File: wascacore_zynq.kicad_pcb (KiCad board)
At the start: 4 copper layers, 67.6 x 31.1 mm, 51 parts, among them J1 SODIMM-200, U1 DDR3, U2 xc7z010clg400

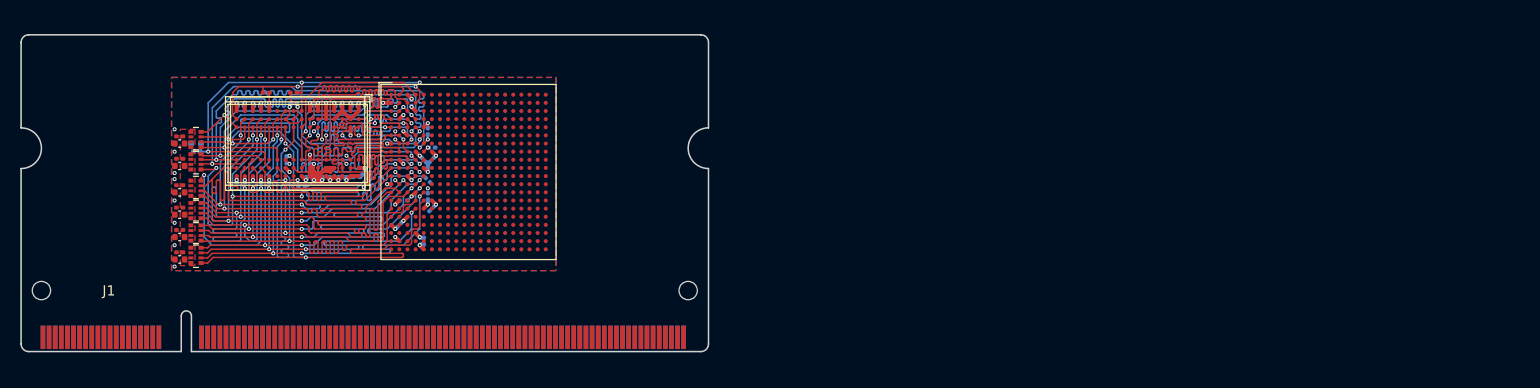
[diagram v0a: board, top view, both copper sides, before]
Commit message: SDRAM added
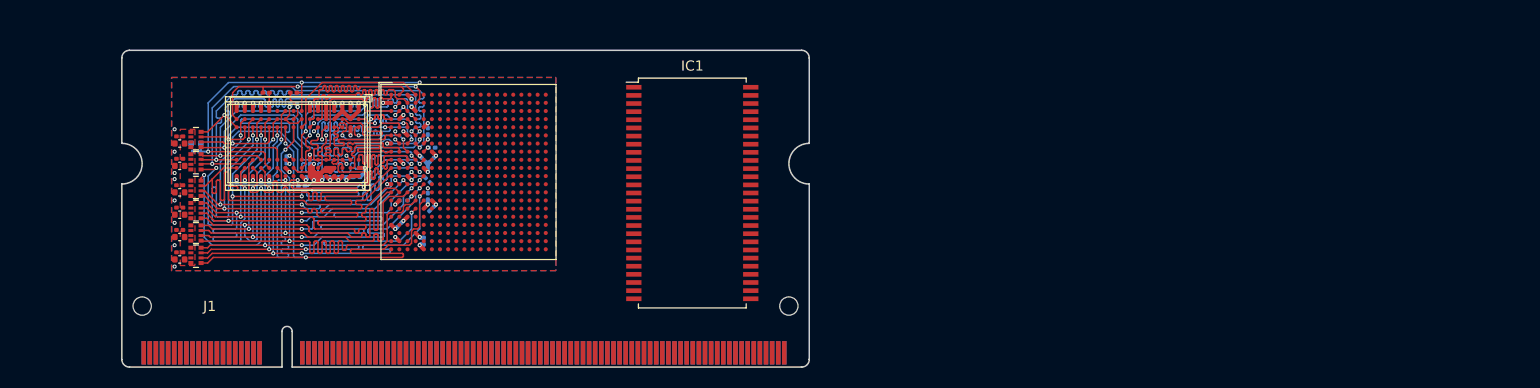
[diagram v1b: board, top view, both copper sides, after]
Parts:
- added IC1: SDRAM_MT48_x16, Package_SO:TSOP-II-54_22.2x10.16mm_P0.8mm, F.Cu at (72.0, 15.4)
- moved J1 10.0 mm to (15.9, 32.5)
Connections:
- U2 pad A10: (no net) -> Net-(U2-PadA10)
- U2 pad A11: (no net) -> Net-(U2-PadA11)
- U2 pad A12: (no net) -> Net-(U2-PadA12)
- U2 pad A13: (no net) -> Net-(U2-PadA13)
- U2 pad A14: (no net) -> Net-(U2-PadA14)
- U2 pad A15: (no net) -> Net-(U2-PadA15)
- U2 pad A16: (no net) -> Net-(U2-PadA16)
- U2 pad A17: (no net) -> Net-(U2-PadA17)
- U2 pad A19: (no net) -> Net-(U2-PadA19)
- U2 pad A20: (no net) -> Net-(U2-PadA20)
- U2 pad A5: (no net) -> Net-(U2-PadA5)
- U2 pad A6: (no net) -> Net-(U2-PadA6)
- U2 pad A7: (no net) -> Net-(U2-PadA7)
- U2 pad A9: (no net) -> Net-(U2-PadA9)
- U2 pad B10: (no net) -> Net-(U2-PadB10)
- U2 pad B12: (no net) -> Net-(U2-PadB12)
- U2 pad B13: (no net) -> Net-(U2-PadB13)
- U2 pad B14: (no net) -> Net-(U2-PadB14)
- U2 pad B15: (no net) -> Net-(U2-PadB15)
- U2 pad B16: (no net) -> Net-(U2-PadA13)
- U2 pad B17: (no net) -> Net-(U2-PadB17)
- U2 pad B18: (no net) -> Net-(U2-PadB18)
- U2 pad B19: (no net) -> Net-(U2-PadB19)
- U2 pad B20: (no net) -> Net-(U2-PadB20)
- U2 pad B5: (no net) -> Net-(U2-PadB5)
- U2 pad B6: (no net) -> Net-(U2-PadB6)
- U2 pad B7: (no net) -> Net-(U2-PadB7)
- U2 pad B8: (no net) -> Net-(U2-PadB8)
- U2 pad B9: (no net) -> Net-(U2-PadB9)
- U2 pad C10: (no net) -> Net-(U2-PadC10)
- U2 pad C11: (no net) -> Net-(U2-PadC11)
- U2 pad C12: (no net) -> Net-(U2-PadC12)
- U2 pad C13: (no net) -> Net-(U2-PadC13)
- U2 pad C15: (no net) -> Net-(U2-PadC15)
- U2 pad C16: (no net) -> Net-(U2-PadC16)
- U2 pad C17: (no net) -> Net-(U2-PadC17)
- U2 pad C18: (no net) -> Net-(U2-PadC18)
- U2 pad C19: (no net) -> Net-(U2-PadC19)
- U2 pad C20: (no net) -> Net-(U2-PadC20)
- U2 pad C5: (no net) -> Net-(U2-PadC5)
- U2 pad C6: (no net) -> Net-(U2-PadC6)
- U2 pad C7: (no net) -> Net-(U2-PadC7)
- U2 pad C8: (no net) -> Net-(U2-PadC8)
- U2 pad D10: (no net) -> Net-(U2-PadD10)
- U2 pad D11: (no net) -> Net-(U2-PadD11)
- U2 pad D12: (no net) -> Net-(U2-PadA13)
- U2 pad D13: (no net) -> Net-(U2-PadD13)
- U2 pad D14: (no net) -> Net-(U2-PadD14)
- U2 pad D15: (no net) -> Net-(U2-PadD15)
- U2 pad D16: (no net) -> Net-(U2-PadD16)
- U2 pad D18: (no net) -> Net-(U2-PadD18)
- U2 pad D19: (no net) -> Net-(U2-PadD19)
- U2 pad D20: (no net) -> Net-(U2-PadD20)
- U2 pad D5: (no net) -> Net-(U2-PadD5)
- U2 pad D6: (no net) -> Net-(U2-PadD6)
- U2 pad D7: (no net) -> Net-(U2-PadB6)
- U2 pad D8: (no net) -> Net-(U2-PadD8)
- U2 pad D9: (no net) -> Net-(U2-PadD9)
- U2 pad E11: (no net) -> Net-(U2-PadE11)
- U2 pad E12: (no net) -> Net-(U2-PadE12)
- U2 pad E13: (no net) -> Net-(U2-PadE13)
- U2 pad E14: (no net) -> Net-(U2-PadE14)
- U2 pad E15: (no net) -> Net-(U2-PadA13)
- U2 pad E16: (no net) -> Net-(U2-PadE16)
- U2 pad E17: (no net) -> Net-(U2-PadE17)
- U2 pad E18: (no net) -> Net-(U2-PadE18)
- U2 pad E19: (no net) -> Net-(U2-PadE19)
- U2 pad E6: (no net) -> Net-(U2-PadE6)
- U2 pad E7: (no net) -> Net-(U2-PadE7)
- U2 pad E8: (no net) -> Net-(U2-PadE8)
- U2 pad E9: (no net) -> Net-(U2-PadE9)
- U2 pad F10: (no net) -> Net-(U2-PadF10)
- U2 pad F11: (no net) -> Net-(U2-PadF11)
- U2 pad F12: (no net) -> Net-(U2-PadF12)
- U2 pad F13: (no net) -> Net-(U2-PadF13)
- U2 pad F14: (no net) -> Net-(U2-PadF14)
- U2 pad F15: (no net) -> Net-(U2-PadF15)
- U2 pad F16: (no net) -> Net-(U2-PadF16)
- U2 pad F17: (no net) -> Net-(U2-PadF17)
- U2 pad F18: (no net) -> Net-(U2-PadC19)
- U2 pad F19: (no net) -> Net-(U2-PadF19)
- U2 pad F20: (no net) -> Net-(U2-PadF20)
- U2 pad F6: (no net) -> Net-(U2-PadF6)
- U2 pad F9: (no net) -> Net-(U2-PadF9)
- U2 pad G14: (no net) -> Net-(U2-PadG14)
- U2 pad G15: (no net) -> Net-(U2-PadG15)
- U2 pad G17: (no net) -> Net-(U2-PadG17)
- U2 pad G18: (no net) -> Net-(U2-PadG18)
- U2 pad G19: (no net) -> Net-(U2-PadG19)
- U2 pad G20: (no net) -> Net-(U2-PadG20)
- U2 pad G6: (no net) -> Net-(U2-PadG6)
- U2 pad H14: (no net) -> Net-(U2-PadC19)
- U2 pad H15: (no net) -> Net-(U2-PadH15)
- U2 pad H16: (no net) -> Net-(U2-PadH16)
- U2 pad H17: (no net) -> Net-(U2-PadH17)
- U2 pad H18: (no net) -> Net-(U2-PadH18)
- U2 pad H20: (no net) -> Net-(U2-PadH20)
- U2 pad J10: (no net) -> Net-(U2-PadJ10)
- U2 pad J14: (no net) -> Net-(U2-PadJ14)
- U2 pad J15: (no net) -> Net-(U2-PadJ15)
- U2 pad J16: (no net) -> Net-(U2-PadJ16)
- U2 pad J17: (no net) -> Net-(U2-PadC19)
- U2 pad J18: (no net) -> Net-(U2-PadJ18)
- U2 pad J19: (no net) -> Net-(U2-PadJ19)
- U2 pad J20: (no net) -> Net-(U2-PadJ20)
- U2 pad J6: (no net) -> Net-(U2-PadJ6)
- U2 pad J9: (no net) -> Net-(U2-PadJ9)
- U2 pad K10: (no net) -> Net-(U2-PadK10)
- U2 pad K14: (no net) -> Net-(U2-PadK14)
- U2 pad K16: (no net) -> Net-(U2-PadK16)
- U2 pad K17: (no net) -> Net-(U2-PadK17)
- U2 pad K18: (no net) -> Net-(U2-PadK18)
- U2 pad K19: (no net) -> Net-(U2-PadK19)
- U2 pad K20: (no net) -> Net-(U2-PadC19)
- U2 pad K6: (no net) -> Net-(U2-PadK6)
- U2 pad K9: (no net) -> Net-(U2-PadK9)
- U2 pad L10: (no net) -> Net-(U2-PadL10)
- U2 pad L14: (no net) -> Net-(U2-PadL14)
- U2 pad L15: (no net) -> Net-(U2-PadL15)
- U2 pad L16: (no net) -> Net-(U2-PadL16)
- U2 pad L17: (no net) -> Net-(U2-PadL17)
- U2 pad L19: (no net) -> Net-(U2-PadL19)
- U2 pad L20: (no net) -> Net-(U2-PadL20)
- U2 pad L6: (no net) -> Net-(U2-PadL6)
- U2 pad L9: (no net) -> Net-(U2-PadL9)
- U2 pad M10: (no net) -> Net-(U2-PadM10)
- U2 pad M14: (no net) -> Net-(U2-PadM14)
- U2 pad M15: (no net) -> Net-(U2-PadM15)
- U2 pad M16: (no net) -> Net-(U2-PadC19)
- U2 pad M17: (no net) -> Net-(U2-PadM17)
- U2 pad M18: (no net) -> Net-(U2-PadM18)
- U2 pad M19: (no net) -> Net-(U2-PadM19)
- U2 pad M20: (no net) -> Net-(U2-PadM20)
- U2 pad M6: (no net) -> Net-(U2-PadM6)
- U2 pad M9: (no net) -> Net-(U2-PadM9)
- U2 pad N15: (no net) -> Net-(U2-PadN15)
- U2 pad N16: (no net) -> Net-(U2-PadN16)
- U2 pad N17: (no net) -> Net-(U2-PadN17)
- U2 pad N18: (no net) -> Net-(U2-PadN18)
- U2 pad N19: (no net) -> Net-(U2-PadN19)
- U2 pad N20: (no net) -> Net-(U2-PadN20)
- U2 pad N6: (no net) -> Net-(U2-PadN6)
- U2 pad P14: (no net) -> Net-(U2-PadP14)
- U2 pad P15: (no net) -> Net-(U2-PadP15)
- U2 pad P16: (no net) -> Net-(U2-PadP16)
- U2 pad P18: (no net) -> Net-(U2-PadP18)
- U2 pad P19: (no net) -> Net-(U2-PadP19)
- U2 pad P20: (no net) -> Net-(U2-PadP20)
- U2 pad R10: (no net) -> Net-(U2-PadR10)
- U2 pad R11: (no net) -> Net-(U2-PadR11)
- U2 pad R14: (no net) -> Net-(U2-PadR14)
- U2 pad R15: (no net) -> Net-(U2-PadN19)
- U2 pad R16: (no net) -> Net-(U2-PadR16)
- U2 pad R17: (no net) -> Net-(U2-PadR17)
- U2 pad R18: (no net) -> Net-(U2-PadR18)
- U2 pad R19: (no net) -> Net-(U2-PadR19)
- U2 pad R6: (no net) -> Net-(U2-PadR6)
- U2 pad T10: (no net) -> Net-(U2-PadT10)
- U2 pad T11: (no net) -> Net-(U2-PadT11)
- U2 pad T12: (no net) -> Net-(U2-PadT12)
- U2 pad T14: (no net) -> Net-(U2-PadT14)
- U2 pad T15: (no net) -> Net-(U2-PadT15)
- U2 pad T16: (no net) -> Net-(U2-PadT16)
- U2 pad T17: (no net) -> Net-(U2-PadT17)
- U2 pad T18: (no net) -> Net-(U2-PadN19)
- U2 pad T19: (no net) -> Net-(U2-PadT19)
- U2 pad T20: (no net) -> Net-(U2-PadT20)
- U2 pad T5: (no net) -> Net-(U2-PadT5)
- U2 pad T6: (no net) -> Net-(U2-PadT6)
- U2 pad T8: (no net) -> Net-(U2-PadT8)
- U2 pad T9: (no net) -> Net-(U2-PadT9)
- U2 pad U10: (no net) -> Net-(U2-PadU10)
- U2 pad U11: (no net) -> Net-(U2-PadT8)
- U2 pad U12: (no net) -> Net-(U2-PadU12)
- U2 pad U13: (no net) -> Net-(U2-PadU13)
- U2 pad U14: (no net) -> Net-(U2-PadU14)
- U2 pad U15: (no net) -> Net-(U2-PadU15)
- U2 pad U17: (no net) -> Net-(U2-PadU17)
- U2 pad U18: (no net) -> Net-(U2-PadU18)
- U2 pad U19: (no net) -> Net-(U2-PadU19)
- U2 pad U20: (no net) -> Net-(U2-PadU20)
- U2 pad U5: (no net) -> Net-(U2-PadU5)
- U2 pad U7: (no net) -> Net-(U2-PadU7)
- U2 pad U8: (no net) -> Net-(U2-PadU8)
- U2 pad U9: (no net) -> Net-(U2-PadU9)
- U2 pad V10: (no net) -> Net-(U2-PadV10)
- U2 pad V11: (no net) -> Net-(U2-PadV11)
- U2 pad V12: (no net) -> Net-(U2-PadV12)
- U2 pad V13: (no net) -> Net-(U2-PadV13)
- U2 pad V14: (no net) -> Net-(U2-PadN19)
- U2 pad V15: (no net) -> Net-(U2-PadV15)
- U2 pad V16: (no net) -> Net-(U2-PadV16)
- U2 pad V17: (no net) -> Net-(U2-PadV17)
- U2 pad V18: (no net) -> Net-(U2-PadV18)
- U2 pad V20: (no net) -> Net-(U2-PadV20)
- U2 pad V5: (no net) -> Net-(U2-PadV5)
- U2 pad V6: (no net) -> Net-(U2-PadV6)
- U2 pad V7: (no net) -> Net-(U2-PadV7)
- U2 pad V8: (no net) -> Net-(U2-PadV8)
- U2 pad W10: (no net) -> Net-(U2-PadW10)
- U2 pad W11: (no net) -> Net-(U2-PadW11)
- U2 pad W13: (no net) -> Net-(U2-PadW13)
- U2 pad W14: (no net) -> Net-(U2-PadW14)
- U2 pad W15: (no net) -> Net-(U2-PadW15)
- U2 pad W16: (no net) -> Net-(U2-PadW16)
- U2 pad W17: (no net) -> Net-(U2-PadN19)
- U2 pad W18: (no net) -> Net-(U2-PadW18)
- U2 pad W19: (no net) -> Net-(U2-PadW19)
- U2 pad W20: (no net) -> Net-(U2-PadW20)
- U2 pad W6: (no net) -> Net-(U2-PadW6)
- U2 pad W7: (no net) -> Net-(U2-PadT8)
- U2 pad W8: (no net) -> Net-(U2-PadW8)
- U2 pad W9: (no net) -> Net-(U2-PadW9)
- U2 pad Y10: (no net) -> Net-(U2-PadT8)
- U2 pad Y11: (no net) -> Net-(U2-PadY11)
- U2 pad Y12: (no net) -> Net-(U2-PadY12)
- U2 pad Y13: (no net) -> Net-(U2-PadY13)
- U2 pad Y14: (no net) -> Net-(U2-PadY14)
- U2 pad Y16: (no net) -> Net-(U2-PadY16)
- U2 pad Y17: (no net) -> Net-(U2-PadY17)
- U2 pad Y18: (no net) -> Net-(U2-PadY18)
- U2 pad Y19: (no net) -> Net-(U2-PadY19)
- U2 pad Y20: (no net) -> Net-(U2-PadN19)
- U2 pad Y6: (no net) -> Net-(U2-PadY6)
- U2 pad Y7: (no net) -> Net-(U2-PadY7)
- U2 pad Y8: (no net) -> Net-(U2-PadY8)
- U2 pad Y9: (no net) -> Net-(U2-PadY9)
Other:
- board size 67.6 x 31.1 mm -> 67.6 x 31.2 mm

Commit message: Routing from wasca board
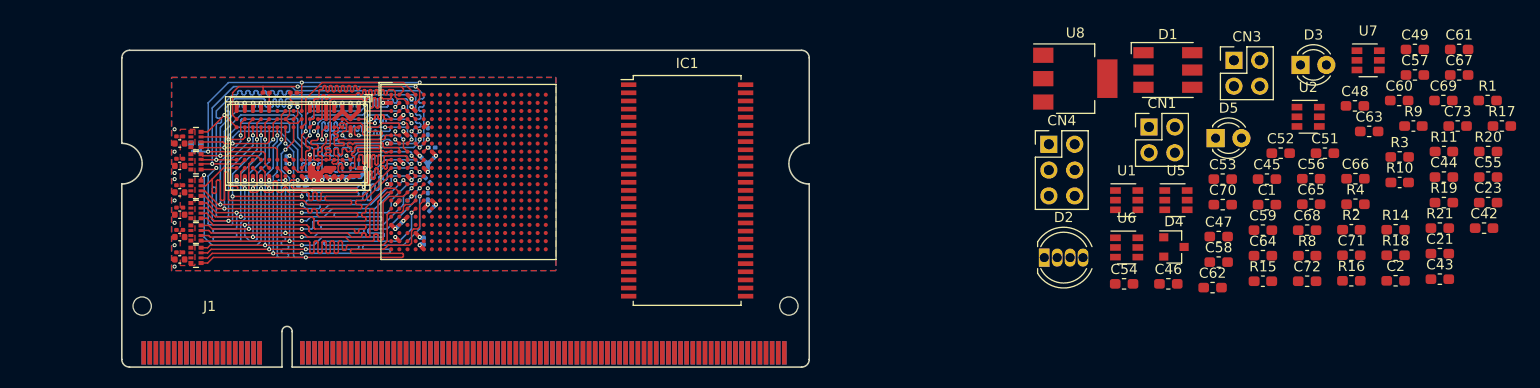
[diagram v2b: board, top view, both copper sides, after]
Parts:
- added C1: 0.1uF, Capacitor_SMD:C_0603_1608Metric_Pad1.05x0.95mm_HandSolder, F.Cu at (128.5, 16.5)
- added C2: 0.1uF, Capacitor_SMD:C_0603_1608Metric_Pad1.05x0.95mm_HandSolder, F.Cu at (141.2, 24.0)
- added C21: 0.1uF, Capacitor_SMD:C_0603_1608Metric_Pad1.05x0.95mm_HandSolder, F.Cu at (145.5, 21.3)
- added C23: 0.1uF, Capacitor_SMD:C_0603_1608Metric_Pad1.05x0.95mm_HandSolder, F.Cu at (150.3, 16.3)
- added C42: 0.1uF, Capacitor_SMD:C_0603_1608Metric_Pad1.05x0.95mm_HandSolder, F.Cu at (149.9, 18.8)
- added C43: 0.1uF, Capacitor_SMD:C_0603_1608Metric_Pad1.05x0.95mm_HandSolder, F.Cu at (145.5, 23.8)
- added C44: 0.1uF, Capacitor_SMD:C_0603_1608Metric_Pad1.05x0.95mm_HandSolder, F.Cu at (145.9, 13.8)
- added C45: 0.1uF, Capacitor_SMD:C_0603_1608Metric_Pad1.05x0.95mm_HandSolder, F.Cu at (128.5, 14.0)
- added C46: 0.1uF, Capacitor_SMD:C_0603_1608Metric_Pad1.05x0.95mm_HandSolder, F.Cu at (118.8, 24.3)
- added C47: 0.1uF, Capacitor_SMD:C_0603_1608Metric_Pad1.05x0.95mm_HandSolder, F.Cu at (123.8, 19.6)
- added C48: 0.1uF, Capacitor_SMD:C_0603_1608Metric_Pad1.05x0.95mm_HandSolder, F.Cu at (137.2, 6.80)
- added C49: 0.1uF, Capacitor_SMD:C_0603_1608Metric_Pad1.05x0.95mm_HandSolder, F.Cu at (143.1, 1.25)
- added C51: 0.1uF, Capacitor_SMD:C_0603_1608Metric_Pad1.05x0.95mm_HandSolder, F.Cu at (134.2, 11.4)
- added C52: 0.1uF, Capacitor_SMD:C_0603_1608Metric_Pad1.05x0.95mm_HandSolder, F.Cu at (129.9, 11.4)
- added C53: 0.1uF, Capacitor_SMD:C_0603_1608Metric_Pad1.05x0.95mm_HandSolder, F.Cu at (124.2, 14.0)
- added C54: 0.1uF, Capacitor_SMD:C_0603_1608Metric_Pad1.05x0.95mm_HandSolder, F.Cu at (114.5, 24.3)
- added C55: 4.7uF, Capacitor_SMD:C_0603_1608Metric_Pad1.05x0.95mm_HandSolder, F.Cu at (150.3, 13.8)
- added C56: 0.1uF, Capacitor_SMD:C_0603_1608Metric_Pad1.05x0.95mm_HandSolder, F.Cu at (132.9, 14.0)
- added C57: 0.1uF, Capacitor_SMD:C_0603_1608Metric_Pad1.05x0.95mm_HandSolder, F.Cu at (143.1, 3.76)
- added C58: 0.1uF, Capacitor_SMD:C_0603_1608Metric_Pad1.05x0.95mm_HandSolder, F.Cu at (123.8, 22.2)
- added C59: 0.1uF, Capacitor_SMD:C_0603_1608Metric_Pad1.05x0.95mm_HandSolder, F.Cu at (128.1, 19.0)
- added C60: 0.1uF, Capacitor_SMD:C_0603_1608Metric_Pad1.05x0.95mm_HandSolder, F.Cu at (141.5, 6.27)
- added C61: 0.1uF, Capacitor_SMD:C_0603_1608Metric_Pad1.05x0.95mm_HandSolder, F.Cu at (147.4, 1.25)
- added C62: 0.1uF, Capacitor_SMD:C_0603_1608Metric_Pad1.05x0.95mm_HandSolder, F.Cu at (123.2, 24.7)
- added C63: 0.1uF, Capacitor_SMD:C_0603_1608Metric_Pad1.05x0.95mm_HandSolder, F.Cu at (138.6, 9.31)
- added C64: 0.1uF, Capacitor_SMD:C_0603_1608Metric_Pad1.05x0.95mm_HandSolder, F.Cu at (128.1, 21.5)
- added C65: 0.1uF, Capacitor_SMD:C_0603_1608Metric_Pad1.05x0.95mm_HandSolder, F.Cu at (132.9, 16.5)
- added C66: 0.1uF, Capacitor_SMD:C_0603_1608Metric_Pad1.05x0.95mm_HandSolder, F.Cu at (137.2, 14.0)
- added C67: 0.1uF, Capacitor_SMD:C_0603_1608Metric_Pad1.05x0.95mm_HandSolder, F.Cu at (147.4, 3.76)
- added C68: 0.1uF, Capacitor_SMD:C_0603_1608Metric_Pad1.05x0.95mm_HandSolder, F.Cu at (132.5, 19.0)
- added C69: 0.1uF, Capacitor_SMD:C_0603_1608Metric_Pad1.05x0.95mm_HandSolder, F.Cu at (145.9, 6.27)
- added C70: 0.1uF, Capacitor_SMD:C_0603_1608Metric_Pad1.05x0.95mm_HandSolder, F.Cu at (124.2, 16.5)
- added C71: 0.1uF, Capacitor_SMD:C_0603_1608Metric_Pad1.05x0.95mm_HandSolder, F.Cu at (136.8, 21.5)
- added C72: 0.1uF, Capacitor_SMD:C_0603_1608Metric_Pad1.05x0.95mm_HandSolder, F.Cu at (132.5, 24.0)
- added C73: 0.1uF, Capacitor_SMD:C_0603_1608Metric_Pad1.05x0.95mm_HandSolder, F.Cu at (147.3, 8.78)
- added CN1: Conn_02x02_Odd_Even, Connector_PinHeader_2.54mm:PinHeader_2x02_P2.54mm_Vertical, F.Cu at (116.9, 8.87)
- added CN3: Conn_02x02_Odd_Even, Connector_PinHeader_2.54mm:PinHeader_2x02_P2.54mm_Vertical, F.Cu at (125.3, 2.32)
- added CN4: Conn_02x03_Odd_Even, Connector_PinHeader_2.54mm:PinHeader_2x03_P2.54mm_Vertical, F.Cu at (107.1, 10.6)
- added D1: LED_RGB, LED_SMD:LED_RGB_5050-6, F.Cu at (118.8, 3.27)
- added D2: LED_BCGR, LED_THT:LED_D5.0mm-4_RGB, F.Cu at (106.6, 21.7)
- added D3: LED, LED_THT:LED_D3.0mm, F.Cu at (131.8, 2.77)
- added D4: BAT54C, Package_TO_SOT_SMD:SOT-23, F.Cu at (119.4, 20.7)
- added D5: LED, LED_THT:LED_D3.0mm, F.Cu at (123.5, 9.97)
- added R1: 1K, Capacitor_SMD:C_0603_1608Metric_Pad1.05x0.95mm_HandSolder, F.Cu at (150.2, 6.27)
- added R10: 470, Capacitor_SMD:C_0603_1608Metric_Pad1.08x0.95mm_HandSolder, F.Cu at (141.6, 14.3)
- added R11: 470, Capacitor_SMD:C_0603_1608Metric_Pad1.08x0.95mm_HandSolder, F.Cu at (145.9, 11.3)
- added R14: 470, Capacitor_SMD:C_0603_1608Metric_Pad1.05x0.95mm_HandSolder, F.Cu at (141.2, 19.0)
- added R15: 5K1, Capacitor_SMD:C_0603_1608Metric_Pad1.08x0.95mm_HandSolder, F.Cu at (128.1, 24.0)
- added R16: 4K7, Capacitor_SMD:C_0603_1608Metric_Pad1.05x0.95mm_HandSolder, F.Cu at (136.8, 24.0)
- added R17: 10K, Capacitor_SMD:C_0603_1608Metric_Pad1.05x0.95mm_HandSolder, F.Cu at (151.6, 8.78)
- added R18: 470, Capacitor_SMD:C_0603_1608Metric_Pad1.05x0.95mm_HandSolder, F.Cu at (141.2, 21.5)
- added R19: 10K, Capacitor_SMD:C_0603_1608Metric_Pad1.05x0.95mm_HandSolder, F.Cu at (145.9, 16.3)
- added R2: 0, Capacitor_SMD:C_0603_1608Metric_Pad1.08x0.95mm_HandSolder, F.Cu at (136.8, 19.0)
- added R20: 10K, Capacitor_SMD:C_0603_1608Metric_Pad1.05x0.95mm_HandSolder, F.Cu at (150.3, 11.3)
- added R21: 10K, Capacitor_SMD:C_0603_1608Metric_Pad1.05x0.95mm_HandSolder, F.Cu at (145.5, 18.8)
- added R3: 10K, Capacitor_SMD:C_0603_1608Metric_Pad1.05x0.95mm_HandSolder, F.Cu at (141.6, 11.8)
- added R4: 10K, Capacitor_SMD:C_0603_1608Metric_Pad1.05x0.95mm_HandSolder, F.Cu at (137.2, 16.5)
- added R8: 470, Capacitor_SMD:C_0603_1608Metric_Pad1.08x0.95mm_HandSolder, F.Cu at (132.5, 21.5)
- added R9: 470, Capacitor_SMD:C_0603_1608Metric_Pad1.08x0.95mm_HandSolder, F.Cu at (142.9, 8.78)
- added U1: SN74LVC1T45DBV, Package_TO_SOT_SMD:SOT-23-6, F.Cu at (114.7, 16.1)
- added U2: SN74LVC1T45DBV, Package_TO_SOT_SMD:SOT-23-6, F.Cu at (132.6, 7.87)
- added U5: SN74LVC1T45DBV, Package_TO_SOT_SMD:SOT-23-6, F.Cu at (119.6, 16.1)
- added U6: SN74LVC1T45DBV, Package_TO_SOT_SMD:SOT-23-6, F.Cu at (114.7, 20.7)
- added U7: SN74LVC1T45DBV, Package_TO_SOT_SMD:SOT-23-6, F.Cu at (138.5, 2.32)
- added U8: LD1117S33TR_SOT223, Package_TO_SOT_SMD:SOT-223-3_TabPin2, F.Cu at (109.7, 4.12)
- moved IC1 0.57 mm to (71.5, 15.1)
- renumbered C8 to C10, C9 to C11, C10 to C12, C11 to C13, C12 to C14, C13 to C15, C14 to C16, C15 to C17, C16 to C18, C17 to C19, C18 to C20, C19 to C22, C20 to C24, C21 to C25, C22 to C26, C23 to C27, C24 to C28, C25 to C29, C1 to C3, C26 to C30, C27 to C31, C28 to C32, C29 to C33, C30 to C34, C31 to C35, C32 to C36, C33 to C37, C34 to C38, C35 to C39, C2 to C4, C36 to C40, C37 to C41, C3 to C5, C4 to C6, C5 to C7, C6 to C8, C7 to C9, R4 to R12, R5 to R13, R1 to R5, R2 to R6, R3 to R7, U1 to U3, U2 to U4
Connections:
- IC1 pad 1: Net-(IC1-Pad1) -> /+3_3V
- IC1 pad 10: Net-(IC1-Pad10) -> /SDR_DQ5
- IC1 pad 11: Net-(IC1-Pad11) -> /SDR_DQ6
- IC1 pad 12: Net-(IC1-Pad12) -> GND
- IC1 pad 13: Net-(IC1-Pad13) -> /SDR_DQ7
- IC1 pad 14: Net-(IC1-Pad14) -> /+3_3V
- IC1 pad 15: Net-(IC1-Pad15) -> /SDR_DQML
- IC1 pad 16: Net-(IC1-Pad16) -> /SDR_WE
- IC1 pad 17: Net-(IC1-Pad17) -> /SDR_CAS
- IC1 pad 18: Net-(IC1-Pad18) -> /SDR_RAS
- IC1 pad 19: Net-(IC1-Pad19) -> /SDR_CS
- IC1 pad 2: Net-(IC1-Pad2) -> /SDR_DQ0
- IC1 pad 20: Net-(IC1-Pad20) -> /SDR_BA0
- IC1 pad 21: Net-(IC1-Pad21) -> /SDR_BA1
- IC1 pad 22: Net-(IC1-Pad22) -> /SDR_A10
- IC1 pad 23: Net-(IC1-Pad23) -> /SDR_A0
- IC1 pad 24: Net-(IC1-Pad24) -> /SDR_A1
- IC1 pad 25: Net-(IC1-Pad25) -> /SDR_A2
- IC1 pad 26: Net-(IC1-Pad26) -> /SDR_A3
- IC1 pad 27: Net-(IC1-Pad27) -> /+3_3V
- IC1 pad 28: Net-(IC1-Pad28) -> GND
- IC1 pad 29: Net-(IC1-Pad29) -> /SDR_A4
- IC1 pad 3: Net-(IC1-Pad3) -> /+3_3V
- IC1 pad 30: Net-(IC1-Pad30) -> /SDR_A5
- IC1 pad 31: Net-(IC1-Pad31) -> /SDR_A6
- IC1 pad 32: Net-(IC1-Pad32) -> /SDR_A7
- IC1 pad 33: Net-(IC1-Pad33) -> /SDR_A8
- IC1 pad 34: Net-(IC1-Pad34) -> /SDR_A9
- IC1 pad 35: Net-(IC1-Pad35) -> /SDR_A11
- IC1 pad 36: Net-(IC1-Pad36) -> /SDR_A12
- IC1 pad 37: Net-(IC1-Pad37) -> /SDR_CKE
- IC1 pad 38: Net-(IC1-Pad38) -> /SDR_CLK
- IC1 pad 39: Net-(IC1-Pad39) -> /SDR_DQMH
- IC1 pad 4: Net-(IC1-Pad4) -> /SDR_DQ1
- IC1 pad 41: Net-(IC1-Pad41) -> GND
- IC1 pad 42: Net-(IC1-Pad42) -> /SDR_DQ8
- IC1 pad 43: Net-(IC1-Pad43) -> /+3_3V
- IC1 pad 44: Net-(IC1-Pad44) -> /SDR_DQ9
- IC1 pad 45: Net-(IC1-Pad45) -> /SDR_DQ10
- IC1 pad 46: Net-(IC1-Pad46) -> GND
- IC1 pad 47: Net-(IC1-Pad47) -> /SDR_DQ11
- IC1 pad 48: Net-(IC1-Pad48) -> /SDR_DQ12
- IC1 pad 49: Net-(IC1-Pad49) -> /+3_3V
- IC1 pad 5: Net-(IC1-Pad5) -> /SDR_DQ2
- IC1 pad 50: Net-(IC1-Pad50) -> /SDR_DQ13
- IC1 pad 51: Net-(IC1-Pad51) -> /SDR_DQ14
- IC1 pad 52: Net-(IC1-Pad52) -> GND
- IC1 pad 53: Net-(IC1-Pad53) -> /SDR_DQ15
- IC1 pad 54: Net-(IC1-Pad54) -> GND
- IC1 pad 6: Net-(IC1-Pad6) -> GND
- IC1 pad 7: Net-(IC1-Pad7) -> /SDR_DQ3
- IC1 pad 8: Net-(IC1-Pad8) -> /SDR_DQ4
- IC1 pad 9: Net-(IC1-Pad9) -> /+3_3V
- J1 pad 1: Net-(J1-Pad1) -> GND
- J1 pad 10: Net-(J1-Pad10) -> /5V
- J1 pad 105: Net-(J1-Pad105) -> GND
- J1 pad 106: Net-(J1-Pad106) -> GND
- J1 pad 107: Net-(J1-Pad107) -> GND
- J1 pad 108: Net-(J1-Pad108) -> GND
- J1 pad 11: Net-(J1-Pad11) -> GND
- J1 pad 12: Net-(J1-Pad12) -> /5V
- J1 pad 157: Net-(J1-Pad157) -> GND
- J1 pad 158: Net-(J1-Pad158) -> GND
- J1 pad 199: Net-(J1-Pad199) -> GND
- J1 pad 2: Net-(J1-Pad2) -> /5V
- J1 pad 200: Net-(J1-Pad200) -> GND
- J1 pad 3: Net-(J1-Pad3) -> GND
- J1 pad 39: Net-(J1-Pad39) -> GND
- J1 pad 4: Net-(J1-Pad4) -> /5V
- J1 pad 40: Net-(J1-Pad40) -> GND
- J1 pad 5: Net-(J1-Pad5) -> GND
- J1 pad 55: Net-(J1-Pad55) -> GND
- J1 pad 56: Net-(J1-Pad56) -> GND
- J1 pad 6: Net-(J1-Pad6) -> /5V
- J1 pad 7: Net-(J1-Pad7) -> GND
- J1 pad 8: Net-(J1-Pad8) -> /5V
- J1 pad 9: Net-(J1-Pad9) -> GND
- U4 pad D18: Net-(U2-PadD18) -> /SDR_A3
- U4 pad D19: Net-(U2-PadD19) -> /SDR_A0
- U4 pad D20: Net-(U2-PadD20) -> /SDR_A1
- U4 pad E17: Net-(U2-PadE17) -> /SDR_A2
- U4 pad E18: Net-(U2-PadE18) -> /SDR_BA1
- U4 pad E19: Net-(U2-PadE19) -> /SDR_A10
- U4 pad F16: Net-(U2-PadF16) -> /SDR_CS
- U4 pad F17: Net-(U2-PadF17) -> /SDR_BA0
- U4 pad F19: Net-(U2-PadF19) -> /SDR_A9
- U4 pad F20: Net-(U2-PadF20) -> /SDR_A8
- U4 pad G15: Net-(U2-PadG15) -> /SDR_DQ11
- U4 pad G17: Net-(U2-PadG17) -> /SDR_A12
- U4 pad G18: Net-(U2-PadG18) -> /SDR_A11
- U4 pad G19: Net-(U2-PadG19) -> /SDR_DQ12
- U4 pad G20: Net-(U2-PadG20) -> /SDR_DQ13
- U4 pad H15: Net-(U2-PadH15) -> /SDR_DQ10
- U4 pad H16: Net-(U2-PadH16) -> /SDR_A5
- U4 pad H17: Net-(U2-PadH17) -> /SDR_A4
- U4 pad H18: Net-(U2-PadH18) -> /SDR_A6
- U4 pad H20: Net-(U2-PadH20) -> /SDR_DQ15
- U4 pad J14: Net-(U2-PadJ14) -> /SDR_DQ9
- U4 pad J18: Net-(U2-PadJ18) -> /SDR_A7
- U4 pad J19: Net-(U2-PadJ19) -> /SDR_DQ5
- U4 pad J20: Net-(U2-PadJ20) -> /SDR_DQ14
- U4 pad K14: Net-(U2-PadK14) -> /SDR_DQ8
- U4 pad K17: Net-(U2-PadK17) -> /SDR_DQ0
- U4 pad K18: Net-(U2-PadK18) -> /SDR_DQ1
- U4 pad K19: Net-(U2-PadK19) -> /SDR_DQ4
- U4 pad L15: Net-(U2-PadL15) -> /SDR_CKE
- U4 pad L16: Net-(U2-PadL16) -> /SDR_DQ2
- U4 pad L17: Net-(U2-PadL17) -> /SDR_DQ3
- U4 pad L19: Net-(U2-PadL19) -> /SDR_DQ6
- U4 pad L20: Net-(U2-PadL20) -> /SDR_DQ7
- U4 pad M17: Net-(U2-PadM17) -> /SDR_DQML
- U4 pad M18: Net-(U2-PadM18) -> /SDR_WE
- U4 pad M19: Net-(U2-PadM19) -> /SDR_CAS
- U4 pad M20: Net-(U2-PadM20) -> /SDR_RAS
- U4 pad N15: Net-(U2-PadN15) -> /SDR_CLK
- U4 pad N16: Net-(U2-PadN16) -> /SDR_DQMH
